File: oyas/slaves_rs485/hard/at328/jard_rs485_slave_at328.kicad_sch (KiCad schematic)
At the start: 59 parts, among them J1 POWER, J5 Prog MSP, U1 BPC_Alim3_3V, U1 MAX485E, U2 MSP430F1232IDW, Y1 8MHz

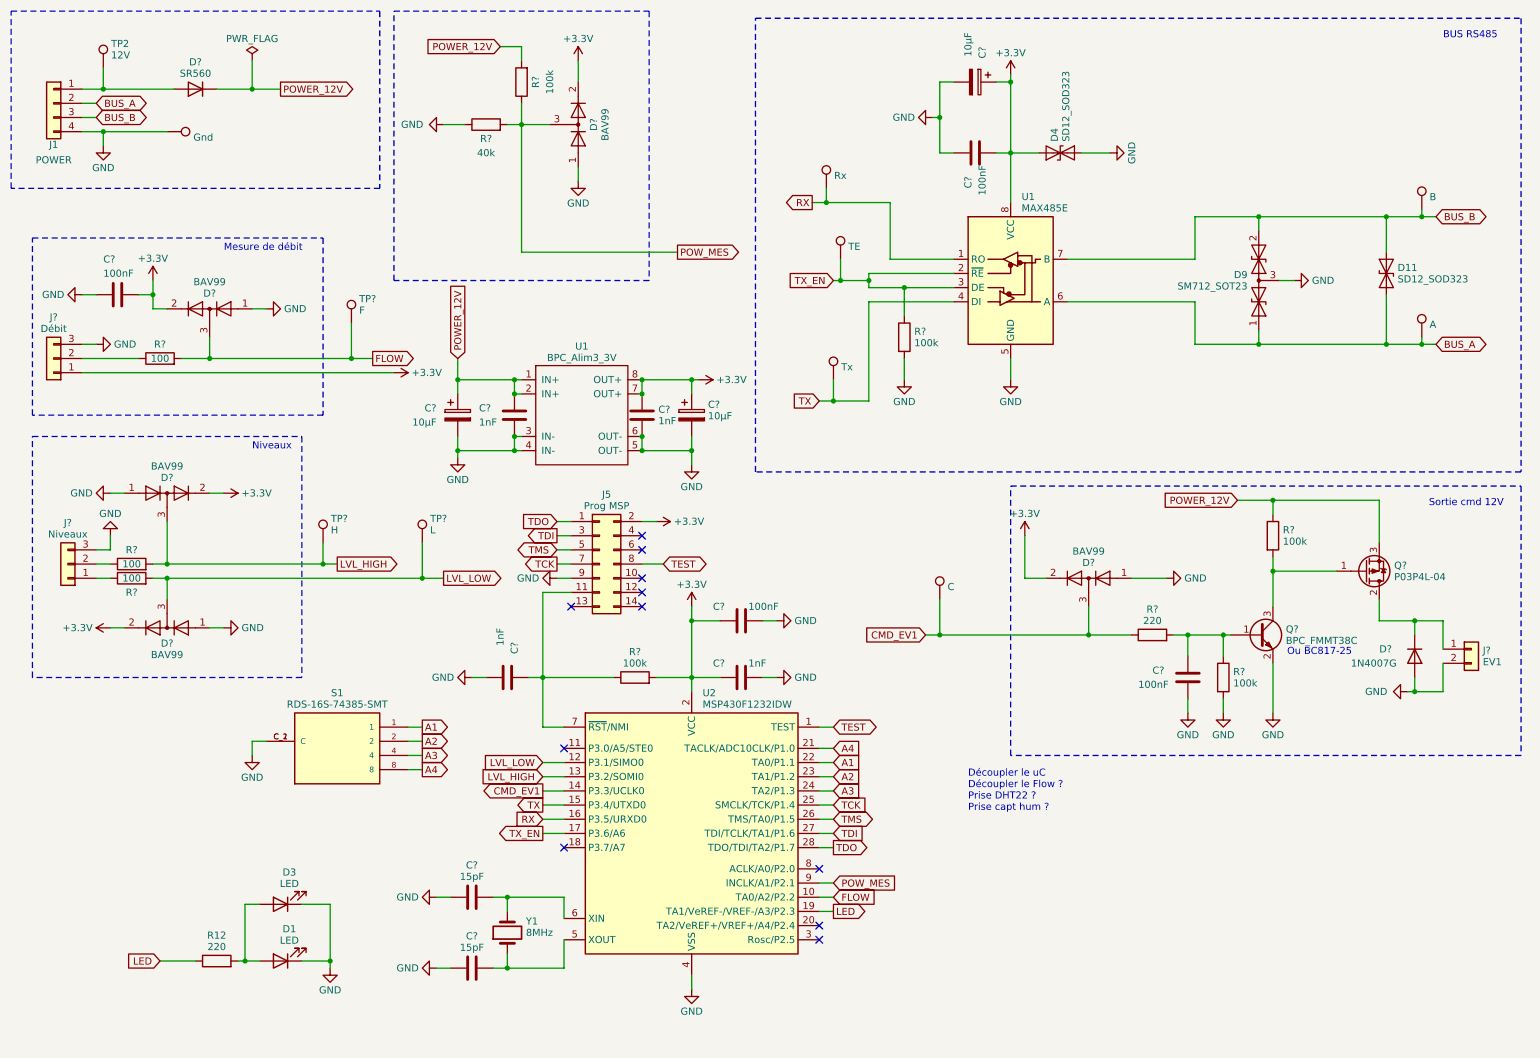
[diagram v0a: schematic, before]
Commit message: Creation carte esclave à base de AT328 (à finir - Connecter power 12V mes, ...)
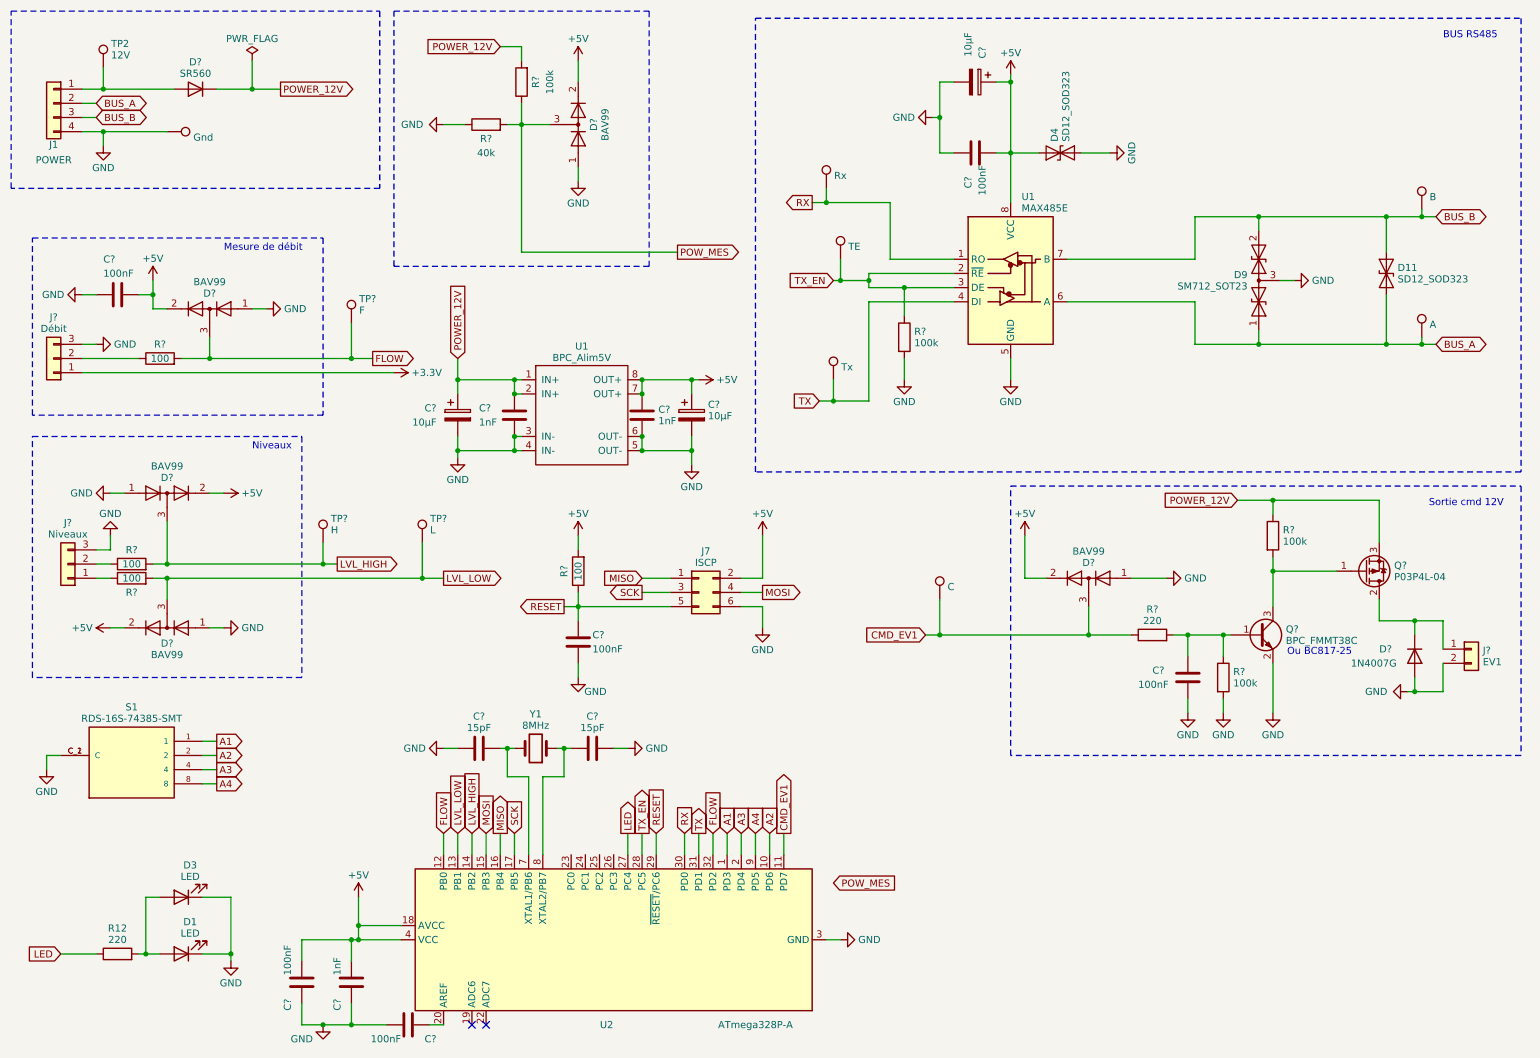
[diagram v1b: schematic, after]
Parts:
- removed C?: 1nF, Capacitor_SMD:C_0805_2012Metric, symbol Device:C
- removed J5: Prog MSP, bpc:BPC_PROG_MSP, symbol bpc:BPC_PROG_MSP
- removed R?: 100k, Resistor_SMD:R_0805_2012Metric_Pad1.20x1.40mm_HandSolder, symbol Device:R
- removed U1: BPC_Alim3_3V, bpc:BPC_Alim3_3V, symbol bpc:BPC_Alim3_3V
- removed U2: MSP430F1232IDW, Package_SO:SOIC-28W_7.5x17.9mm_P1.27mm, symbol MCU_Texas_MSP430:MSP430F1232IDW
- added C? (x2): 100nF, Capacitor_SMD:C_0805_2012Metric, symbol Device:C
- added J7: ISCP, bpc:BPC_ISCP_CMS, symbol bpc:BPC_ISCP
- added R?: 100, Resistor_SMD:R_0805_2012Metric_Pad1.20x1.40mm_HandSolder, symbol Device:R
- added U1: BPC_Alim5V, bpc:BPC_Alim5V, symbol bpc:BPC_Alim5V
- added U2: ATmega328P-A, Package_QFP:TQFP-32_7x7mm_P0.8mm, symbol MCU_Microchip_ATmega:ATmega328P-A
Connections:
- net +3.3V: no longer C?.1, C?.1, C?.1, C?.1, C?.2, C?.2, C?.2, D4.1 (A1), D?.2 (A), D?.2 (A), D?.2 (A), D?.2 (A), D?.2 (A), U1.8 (VCC)
- net A1: now also U2.1 (PD3)
- net A2: now also U2.10 (PD6)
- net A3: now also U2.2 (PD4)
- net A4: now also U2.9 (PD5)
- net CMD_EV1: now also U2.11 (PD7)
- net FLOW: now also U2.12 (PB0), U2.32 (PD2)
- net GND: now also C?.2, C?.2, C?.2, C?.1, C?.2, J7.6 (GND), U1.3 (IN-), U1.4 (IN-), U1.5 (OUT-), U1.6 (OUT-), U2.21 (GND), U2.3 (GND), U2.5 (GND); no longer C?.1, C?.1, C?.1
- net LED: now also U2.27 (PC4)
- net LVL_HIGH: now also U2.14 (PB2)
- net LVL_LOW: now also U2.13 (PB1)
- net POWER_12V: now also U1.1 (IN+), U1.2 (IN+)
- net RX: now also U2.30 (PD0)
- net TX: now also U2.31 (PD1)
- net TX_EN: now also U2.28 (PC5)
- net at C?.2: now also Y1.2, U2.7 (XTAL1/PB6); no longer Y1.1
- new net: C?.2, U2.20 (AREF)
- new net: C?.1, U2.8 (XTAL2/PB7), Y1.1
- new net +5V: C?.1, C?.1, C?.1, C?.1, C?.1, C?.1, C?.2, D4.1 (A1), D?.2 (A), D?.2 (A), D?.2 (A), D?.2 (A), D?.2 (A), J7.2 (VCC), R?.2, U1.7 (OUT+), U1.8 (OUT+), U1.8 (VCC), U2.18 (AVCC), U2.4 (VCC), U2.6 (VCC)
- new net MISO: J7.1 (MISO), U2.16 (PB4)
- new net MOSI: J7.4 (MOSI), U2.15 (PB3)
- new net RESET: C?.1, J7.5 (RST), R?.1, U2.29 (~{RESET}/PC6)
- new net SCK: J7.3 (SCK), U2.17 (PB5)
- no-connect marks 11 -> 2
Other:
- note removed: "Découpler le uC Découpler le Flow ? Prise DHT22 ? Prise capt hum ?"
- title: Esclave Oya MSP430 -> Esclave Oya AT328
- moved on the sheet: C?, D1, D3, R12, S1, Y1

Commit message: Finalisation carte AT328
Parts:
- C? (x2): value 15pF -> 10pF
- Y1: Farnel 4235681 -> 4242855; RefFab ABM8AAIG-8.000MHZ-V2R-T -> ABM8AAIG-8.000MHZ-V2R-T3
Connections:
- net +3.3V is gone; now on net +5V: J?.1 (Pin_1)
- net POW_MES: now also U2.25 (PC2)
- no-connect marks 2 -> 5
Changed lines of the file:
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@@
   )
   (no_connect (at 97.79 194.31))
+  (no_connect (at 120.65 163.83))
+  (no_connect (at 115.57 163.83))
+  (no_connect (at 113.03 163.83))
   (no_connect (at 95.25 194.31))
   (wire (pts (xy 55.88 26.67) (xy 60.96 26.67))
@@
     (stroke (width 0) (type default))
   )
+  (wire (pts (xy 118.11 160.02) (xy 118.11 163.83))
+    (stroke (width 0) (type default))
+  )
   (wire (pts (xy 264.16 132.08) (xy 264.16 134.62))
     (stroke (width 0) (type default))
@@
     )
   )
-  (global_label "POW_MES" (shape input) (at 160.02 168.91 0) (fields_autoplaced)
+  (global_label "POW_MES" (shape input) (at 118.11 160.02 90) (fields_autoplaced)
     (effects (font (size 1.27 1.27)) (justify left))
-    (property "Intersheetrefs" "${INTERSHEET_REFS}" (at 171.7552 168.91 0)
+    (property "Intersheetrefs" "${INTERSHEET_REFS}" (at 118.11 148.2848 90)
       (effects (font (size 1.27 1.27)) (justify left) hide)
     )
@@
   (symbol (lib_id "Device:C") (at 83.82 194.31 90) (unit 1)
     (in_bom yes) (on_board yes) (dnp no)
-    (property "Reference" "C?" (at 88.9 196.85 90)
+    (property "Reference" "C?" (at 82.55 195.58 90)
       (effects (font (size 1.27 1.27)) (justify left))
     )
-    (property "Value" "100nF" (at 82.55 196.85 90)
+    (property "Value" "100nF" (at 91.44 195.58 90)
       (effects (font (size 1.27 1.27)) (justify left))
     )
@@
   (symbol (lib_id "Device:C") (at 64.77 186.69 0) (unit 1)
     (in_bom yes) (on_board yes) (dnp no)
-    (property "Reference" "C?" (at 62.23 191.77 90)
+    (property "Reference" "C?" (at 67.31 185.42 90)
       (effects (font (size 1.27 1.27)) (justify left))
     )
-    (property "Value" "100nF" (at 62.23 185.42 90)
+    (property "Value" "100nF" (at 69.85 185.42 90)
       (effects (font (size 1.27 1.27)) (justify left))
     )
@@
     )
   )
+  (symbol (lib_id "power:+5V") (at 38.1 60.96 0) (unit 1)
+    (in_bom yes) (on_board yes) (dnp no) (fields_autoplaced)
+    (property "Reference" "#PWR022" (at 38.1 64.77 0)
+      (effects (font (size 1.27 1.27)) hide)
+    )
+    (property "Value" "+5V" (at 38.1 57.015 0)
+      (effects (font (size 1.27 1.27)))
+    )
+    (property "Footprint" "" (at 38.1 60.96 0)
+      (effects (font (size 1.27 1.27)) hide)
+    )
+    (property "Datasheet" "" (at 38.1 60.96 0)
+      (effects (font (size 1.27 1.27)) hide)
+    )
+    (pin "1")
+    (instances
+      (project "jard_rs485_slave_at328"
+        (path "/a198b99e-c4dc-4064-b4d8-b20710c7a061"
+          (reference "#PWR022") (unit 1)
+        )
+      )
+    )
+  )
   (symbol (lib_id "Device:C") (at 96.52 144.78 90) (unit 1)
     (in_bom yes) (on_board yes) (dnp no)
@@
       (effects (font (size 1.27 1.27)))
     )
-    (property "Value" "15pF" (at 96.52 141.089 90)
+    (property "Value" "10pF" (at 96.52 141.089 90)
       (effects (font (size 1.27 1.27)))
     )
@@
   (symbol (lib_id "Device:C") (at 73.66 186.69 0) (unit 1)
     (in_bom yes) (on_board yes) (dnp no)
-    (property "Reference" "C?" (at 71.12 191.77 90)
+    (property "Reference" "C?" (at 76.2 185.42 90)
       (effects (font (size 1.27 1.27)) (justify left))
     )
-    (property "Value" "1nF" (at 71.12 185.42 90)
+    (property "Value" "1nF" (at 78.74 185.42 90)
       (effects (font (size 1.27 1.27)) (justify left))
     )
@@
       (effects (font (size 1.27 1.27)) hide)
     )
-    (property "Farnel" "4235681" (at 106.68 151.13 0)
+    (property "Farnel" "4242855" (at 106.68 151.13 0)
       (effects (font (size 1.27 1.27)) hide)
     )
-    (property "RefFab" "ABM8AAIG-8.000MHZ-V2R-T" (at 108.728 141.4526 90)
+    (property "RefFab" "ABM8AAIG-8.000MHZ-V2R-T3" (at 108.728 141.4526 90)
       (effects (font (size 1.27 1.27)) (justify right) hide)
     )
@@
     )
   )
-  (symbol (lib_id "power:+3.3V") (at 81.28 77.47 270) (unit 1)
-    (in_bom yes) (on_board yes) (dnp no) (fields_autoplaced)
-    (property "Reference" "#PWR022" (at 77.47 77.47 0)
-      (effects (font (size 1.27 1.27)) hide)
-    )
-    (property "Value" "+3.3V" (at 84.455 77.47 90)
-      (effects (font (size 1.27 1.27)) (justify left))
-    )
-    (property "Footprint" "" (at 81.28 77.47 0)
-      (effects (font (size 1.27 1.27)) hide)
-    )
-    (property "Datasheet" "" (at 81.28 77.47 0)
-      (effects (font (size 1.27 1.27)) hide)
-    )
-    (pin "1")
-    (instances
-      (project "jard_rs485_slave_at328"
-        (path "/a198b99e-c4dc-4064-b4d8-b20710c7a061"
-          (reference "#PWR022") (unit 1)
-        )
-      )
-    )
-  )
   (symbol (lib_id "power:GND") (at 19.05 148.59 0) (unit 1)
     (in_bom yes) (on_board yes) (dnp no) (fields_autoplaced)
@@
       (effects (font (size 1.27 1.27)))
     )
-    (property "Value" "15pF" (at 116.84 141.089 90)
+    (property "Value" "10pF" (at 116.84 141.089 90)
       (effects (font (size 1.27 1.27)))
     )
@@
     )
   )
-  (symbol (lib_id "power:+5V") (at 38.1 60.96 0) (unit 1)
+  (symbol (lib_id "power:+5V") (at 81.28 77.47 270) (unit 1)
     (in_bom yes) (on_board yes) (dnp no) (fields_autoplaced)
-    (property "Reference" "#PWR042" (at 38.1 64.77 0)
+    (property "Reference" "#PWR042" (at 77.47 77.47 0)
       (effects (font (size 1.27 1.27)) hide)
     )
-    (property "Value" "+5V" (at 38.1 57.015 0)
-      (effects (font (size 1.27 1.27)))
+    (property "Value" "+5V" (at 84.455 77.47 90)
+      (effects (font (size 1.27 1.27)) (justify left))
     )
-    (property "Footprint" "" (at 38.1 60.96 0)
+    (property "Footprint" "" (at 81.28 77.47 0)
       (effects (font (size 1.27 1.27)) hide)
     )
-    (property "Datasheet" "" (at 38.1 60.96 0)
+    (property "Datasheet" "" (at 81.28 77.47 0)
       (effects (font (size 1.27 1.27)) hide)
     )
